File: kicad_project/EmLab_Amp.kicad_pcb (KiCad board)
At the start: 4 copper layers, 118.1 x 58 mm, 179 parts, among them J1 JTAG, J2 USB_C_Receptacle, J3 GPIO_EXP, J4 BNC, U1 TPS7A80, U10 THS4131ID, U11 THS4131ID, U12 THS4131ID, U2 LT3094xDD, U3 LT3045xDD, U4 TPS6513x, U5 LPC4370-TFBGA100, U6 IS25LP080D, U7 ADR421, U8 MCP601R, U9 LMH6518, Y1 12MHz Crystal

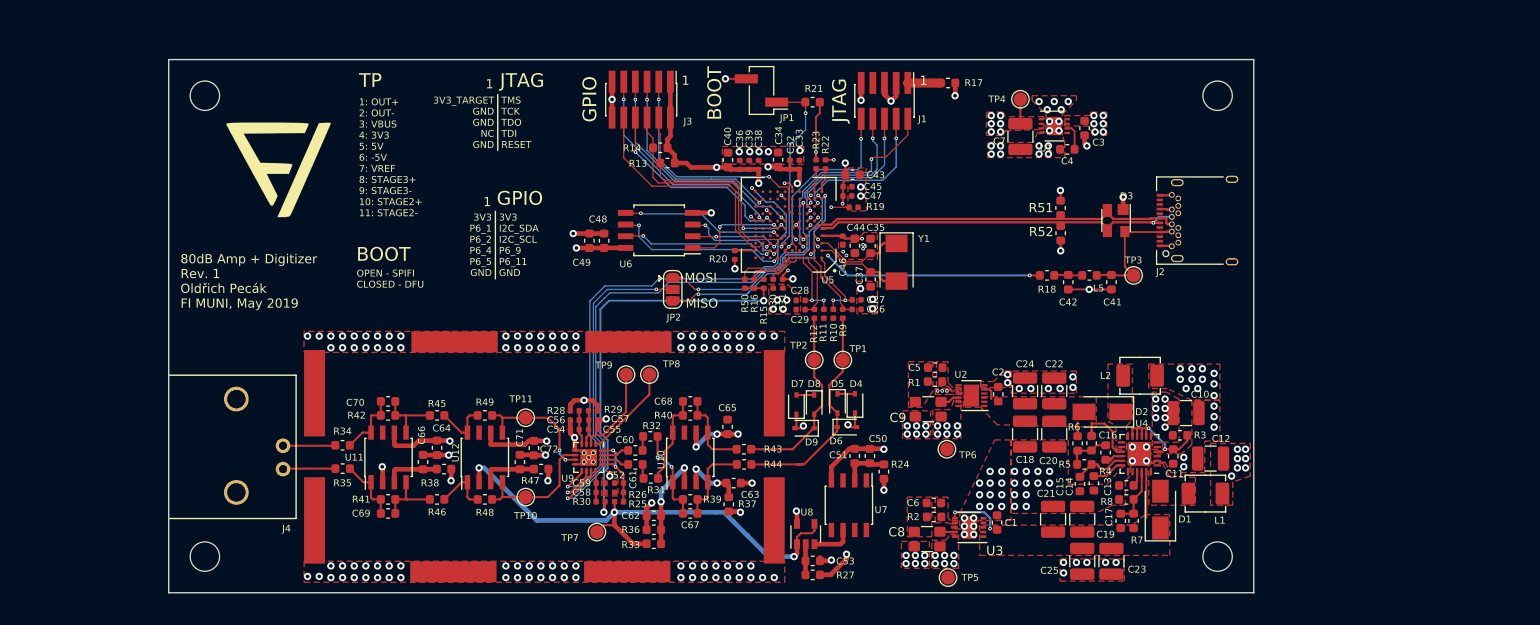
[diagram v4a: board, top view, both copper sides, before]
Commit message: PCB - add GND test points
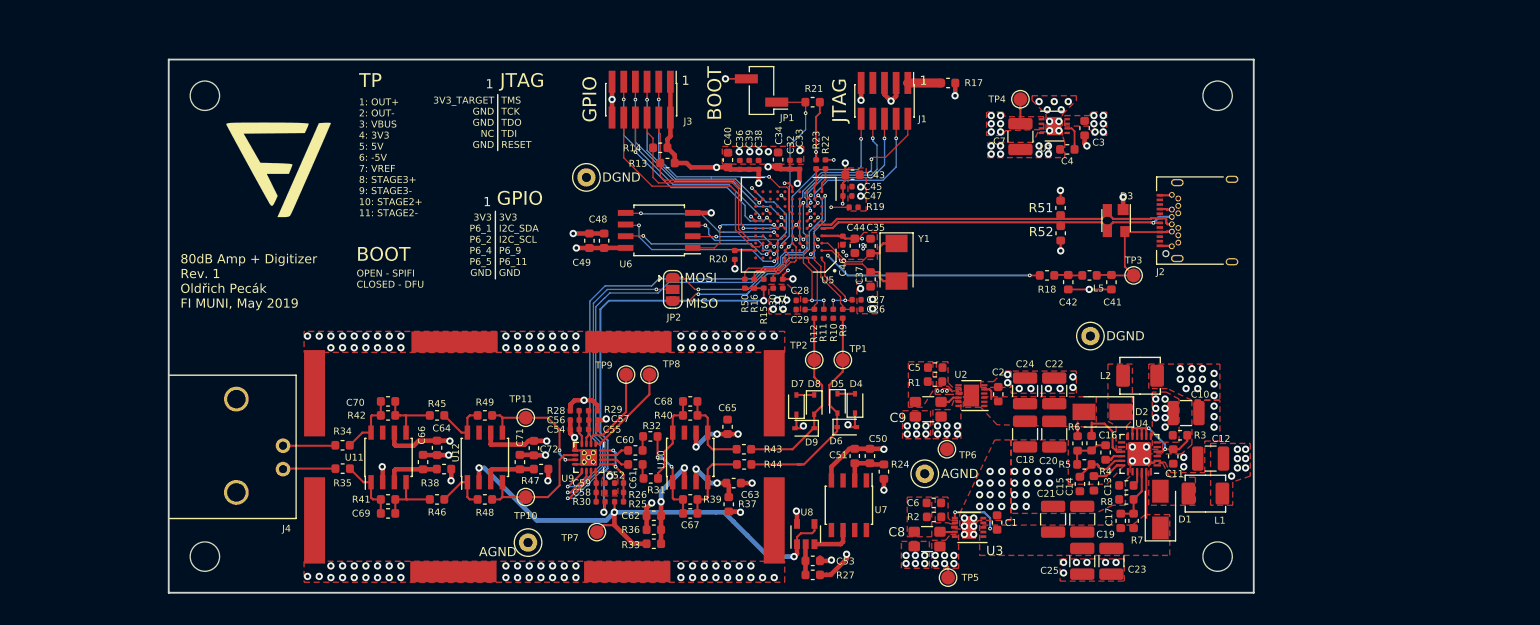
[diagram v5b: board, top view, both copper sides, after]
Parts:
- added AGND: TestPoint_Loop_D1.80mm_Drill1.0mm_Beaded, TestPoint:TestPoint_Loop_D1.80mm_Drill1.0mm_Beaded, F.Cu at (163.7, 105.7)
- added AGND: TestPoint_Loop_D1.80mm_Drill1.0mm_Beaded, TestPoint:TestPoint_Loop_D1.80mm_Drill1.0mm_Beaded, F.Cu at (120.5, 113.2)
- added DGND: TestPoint_Loop_D1.80mm_Drill1.0mm_Beaded, TestPoint:TestPoint_Loop_D1.80mm_Drill1.0mm_Beaded, F.Cu at (126.9, 73.4)
- added DGND: TestPoint_Loop_D1.80mm_Drill1.0mm_Beaded, TestPoint:TestPoint_Loop_D1.80mm_Drill1.0mm_Beaded, F.Cu at (181.7, 90.7)
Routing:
- net +5V: track 15.6 -> 17.3 mm
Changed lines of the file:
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@@
-(kicad_pcb (version 20171130) (host pcbnew "(5.0.0)")
+(kicad_pcb (version 20171130) (host pcbnew 5.0.0+dfsg1-2~bpo9+1)
   (general
     (thickness 1.6)
     (drawings 35)
-    (tracks 1476)
+    (tracks 1478)
     (zones 0)
-    (modules 179)
+    (modules 183)
     (nets 170)
   )
@@
   )
   (setup
-    (last_trace_width 0.244)
+    (last_trace_width 0.2)
     (user_trace_width 0.125)
     (user_trace_width 0.244)
@@
     (trace_min 0.125)
     (segment_width 0.15)
-    (edge_width 0.15)
+    (edge_width 0.2)
     (via_size 0.4)
     (via_drill 0.2)
@@
     (mod_text_size 0.75 0.75)
     (mod_text_width 0.135)
-    (pad_size 2.6 2.6)
-    (pad_drill 0)
+    (pad_size 2 2)
+    (pad_drill 1)
     (pad_to_mask_clearance 0.1)
     (solder_mask_min_width 0.15)
@@
     (add_net "Net-(U7-Pad8)")
   )
+  (module TestPoint:TestPoint_Loop_D1.80mm_Drill1.0mm_Beaded locked (layer F.Cu)
+    (at 126.873 73.406)
+    (descr "wire loop with bead as test point, loop diameter 1.8mm, hole diameter 1.0mm")
+    (tags "test point wire loop bead")
+    (fp_text reference DGND (at 3.81 0) (layer F.SilkS)
+      (effects (font (size 1 1) (thickness 0.15)))
+    )
+    (fp_text value TestPoint_Loop_D1.80mm_Drill1.0mm_Beaded (at 0 -2.8) (layer F.Fab)
+      (effects (font (size 1 1) (thickness 0.15)))
+    )
+    (fp_circle (center 0 0) (end 1.8 0) (layer F.CrtYd) (width 0.05))
+    (fp_circle (center 0 0) (end 1.5 0) (layer F.SilkS) (width 0.12))
+    (fp_line (start -0.9 -0.2) (end 0.9 -0.2) (layer F.Fab) (width 0.12))
+    (fp_line (start 0.9 -0.2) (end 0.9 0.2) (layer F.Fab) (width 0.12))
+    (fp_line (start 0.9 0.2) (end -0.9 0.2) (layer F.Fab) (width 0.12))
+    (fp_line (start -0.9 0.2) (end -0.9 -0.2) (layer F.Fab) (width 0.12))
+    (fp_circle (center 0 0) (end 1.3 0) (layer F.Fab) (width 0.12))
+    (fp_text user %R (at 0.7 2.5) (layer F.Fab)
+      (effects (font (size 1 1) (thickness 0.15)))
+    )
+    (pad 1 thru_hole circle (at 0 0) (size 2 2) (drill 1) (layers *.Cu *.Mask)
+      (net 19 GND))
+    (model ${KISYS3DMOD}/TestPoint.3dshapes/TestPoint_Loop_D1.80mm_Drill1.0mm_Beaded.wrl
+      (at (xyz 0 0 0))
+      (scale (xyz 1 1 1))
+      (rotate (xyz 0 0 0))
+    )
+  )
+  (module TestPoint:TestPoint_Loop_D1.80mm_Drill1.0mm_Beaded locked (layer F.Cu)
+    (at 181.737 90.678)
+    (descr "wire loop with bead as test point, loop diameter 1.8mm, hole diameter 1.0mm")
+    (tags "test point wire loop bead")
+    (fp_text reference DGND (at 3.81 0) (layer F.SilkS)
+      (effects (font (size 1 1) (thickness 0.15)))
+    )
+    (fp_text value TestPoint_Loop_D1.80mm_Drill1.0mm_Beaded (at 0 -2.8) (layer F.Fab)
+      (effects (font (size 1 1) (thickness 0.15)))
+    )
+    (fp_text user %R (at 0.7 2.5) (layer F.Fab)
+      (effects (font (size 1 1) (thickness 0.15)))
+    )
+    (fp_circle (center 0 0) (end 1.3 0) (layer F.Fab) (width 0.12))
+    (fp_line (start -0.9 0.2) (end -0.9 -0.2) (layer F.Fab) (width 0.12))
+    (fp_line (start 0.9 0.2) (end -0.9 0.2) (layer F.Fab) (width 0.12))
+    (fp_line (start 0.9 -0.2) (end 0.9 0.2) (layer F.Fab) (width 0.12))
+    (fp_line (start -0.9 -0.2) (end 0.9 -0.2) (layer F.Fab) (width 0.12))
+    (fp_circle (center 0 0) (end 1.5 0) (layer F.SilkS) (width 0.12))
+    (fp_circle (center 0 0) (end 1.8 0) (layer F.CrtYd) (width 0.05))
+    (pad 1 thru_hole circle (at 0 0) (size 2 2) (drill 1) (layers *.Cu *.Mask)
+      (net 19 GND))
+    (model ${KISYS3DMOD}/TestPoint.3dshapes/TestPoint_Loop_D1.80mm_Drill1.0mm_Beaded.wrl
+      (at (xyz 0 0 0))
+      (scale (xyz 1 1 1))
+      (rotate (xyz 0 0 0))
+    )
+  )
+  (module TestPoint:TestPoint_Loop_D1.80mm_Drill1.0mm_Beaded locked (layer F.Cu)
+    (at 163.703 105.664)
+    (descr "wire loop with bead as test point, loop diameter 1.8mm, hole diameter 1.0mm")
+    (tags "test point wire loop bead")
+    (fp_text reference AGND (at 3.81 0) (layer F.SilkS)
+      (effects (font (size 1 1) (thickness 0.15)))
+    )
+    (fp_text value TestPoint_Loop_D1.80mm_Drill1.0mm_Beaded (at 0 -2.8) (layer F.Fab)
+      (effects (font (size 1 1) (thickness 0.15)))
+    )
+    (fp_circle (center 0 0) (end 1.8 0) (layer F.CrtYd) (width 0.05))
+    (fp_circle (center 0 0) (end 1.5 0) (layer F.SilkS) (width 0.12))
+    (fp_line (start -0.9 -0.2) (end 0.9 -0.2) (layer F.Fab) (width 0.12))
+    (fp_line (start 0.9 -0.2) (end 0.9 0.2) (layer F.Fab) (width 0.12))
+    (fp_line (start 0.9 0.2) (end -0.9 0.2) (layer F.Fab) (width 0.12))
+    (fp_line (start -0.9 0.2) (end -0.9 -0.2) (layer F.Fab) (width 0.12))
+    (fp_circle (center 0 0) (end 1.3 0) (layer F.Fab) (width 0.12))
+    (fp_text user %R (at 0.7 2.5) (layer F.Fab)
+      (effects (font (size 1 1) (thickness 0.15)))
+    )
+    (pad 1 thru_hole circle (at 0 0) (size 2 2) (drill 1) (layers *.Cu *.Mask)
+      (net 19 GND))
+    (model ${KISYS3DMOD}/TestPoint.3dshapes/TestPoint_Loop_D1.80mm_Drill1.0mm_Beaded.wrl
+      (at (xyz 0 0 0))
+      (scale (xyz 1 1 1))
+      (rotate (xyz 0 0 0))
+    )
+  )
   (module MountingHole:MountingHole_3.2mm_M3 (layer F.Cu)
     (at 85.344 114.681)
@@
       (xy 5.063436 -5.054887) (xy 5.430622 -5.062373) (xy 5.666926 -5.040026)) (layer F.SilkS) (width 0.01))
   )
+  (module TestPoint:TestPoint_Loop_D1.80mm_Drill1.0mm_Beaded locked (layer F.Cu)
+    (at 120.523 113.157)
+    (descr "wire loop with bead as test point, loop diameter 1.8mm, hole diameter 1.0mm")
+    (tags "test point wire loop bead")
+    (fp_text reference AGND (at -3.302 1.016) (layer F.SilkS)
+      (effects (font (size 1 1) (thickness 0.15)))
+    )
+    (fp_text value TestPoint_Loop_D1.80mm_Drill1.0mm_Beaded (at 0 -2.8) (layer F.Fab)
+      (effects (font (size 1 1) (thickness 0.15)))
+    )
+    (fp_text user %R (at 0.7 2.5) (layer F.Fab)
+      (effects (font (size 1 1) (thickness 0.15)))
+    )
+    (fp_circle (center 0 0) (end 1.3 0) (layer F.Fab) (width 0.12))
+    (fp_line (start -0.9 0.2) (end -0.9 -0.2) (layer F.Fab) (width 0.12))
+    (fp_line (start 0.9 0.2) (end -0.9 0.2) (layer F.Fab) (width 0.12))
+    (fp_line (start 0.9 -0.2) (end 0.9 0.2) (layer F.Fab) (width 0.12))
+    (fp_line (start -0.9 -0.2) (end 0.9 -0.2) (layer F.Fab) (width 0.12))
+    (fp_circle (center 0 0) (end 1.5 0) (layer F.SilkS) (width 0.12))
+    (fp_circle (center 0 0) (end 1.8 0) (layer F.CrtYd) (width 0.05))
+    (pad 1 thru_hole circle (at 0 0) (size 2 2) (drill 1) (layers *.Cu *.Mask)
+      (net 19 GND))
+    (model ${KISYS3DMOD}/TestPoint.3dshapes/TestPoint_Loop_D1.80mm_Drill1.0mm_Beaded.wrl
+      (at (xyz 0 0 0))
+      (scale (xyz 1 1 1))
+      (rotate (xyz 0 0 0))
+    )
+  )
   (gr_text MISO (at 139.446 87.122) (layer F.SilkS)
     (effects (font (size 1 1) (thickness 0.2)))
@@
     (arrow2b (pts (xy 199.517 53.721) (xy 198.390496 54.307421)))
   )
-  (gr_line (start 199.517 118.618) (end 81.407 118.618) (layer Edge.Cuts) (width 0.15))
-  (gr_line (start 199.517 60.579) (end 199.517 118.618) (layer Edge.Cuts) (width 0.15))
-  (gr_line (start 81.407 60.579) (end 199.517 60.579) (layer Edge.Cuts) (width 0.15))
-  (gr_line (start 81.407 118.618) (end 81.407 60.579) (layer Edge.Cuts) (width 0.15))
+  (gr_line (start 199.517 118.618) (end 81.407 118.618) (layer Edge.Cuts) (width 0.2))
+  (gr_line (start 199.517 60.579) (end 199.517 118.618) (layer Edge.Cuts) (width 0.2))
+  (gr_line (start 81.407 60.579) (end 199.517 60.579) (layer Edge.Cuts) (width 0.2))
+  (gr_line (start 81.407 118.618) (end 81.407 60.579) (layer Edge.Cuts) (width 0.2))
   (gr_line (start 147.32 116.332) (end 147.32 91.313) (layer Dwgs.User) (width 0.2))
   (gr_line (start 97.282 116.332) (end 147.32 116.332) (layer Dwgs.User) (width 0.2))
@@
   (segment (start 153.459 116.67) (end 155.194 114.935) (width 0.5) (layer F.Cu) (net 8))
   (segment (start 155.194 114.935) (end 155.194 114.427) (width 0.5) (layer F.Cu) (net 8))
+  (segment (start 166.243 115.824) (end 165.862 115.443) (width 0.244) (layer F.Cu) (net 8))
+  (segment (start 166.243 116.967) (end 166.243 115.824) (width 0.244) (layer F.Cu) (net 8))
   (segment (start 128.81366 81.0768) (end 128.80086 81.0896) (width 0.5) (layer F.Cu) (net 9))
   (segment (start 131.14526 81.0768) (end 128.81366 81.0768) (width 0.5) (layer F.Cu) (net 9))
@@
       )
     )
+  )
+  (zone (net 0) (net_name "") (layer In2.Cu) (hatch edge 0.508)
+    (connect_pads (clearance 0.2))
+    (min_thickness 0.254)
+    (keepout (tracks not_allowed) (vias not_allowed) (copperpour not_allowed))
+    (fill (arc_segments 16) (thermal_gap 0.508) (thermal_bridge_width 0.508))
+    (polygon
+      (pts
+        (xy 141.605 100.711) (xy 141.605 101.981) (xy 140.462 101.981) (xy 139.065 103.378) (xy 138.176 103.378)
+        (xy 138.176 102.235) (xy 140.081 100.711)
+      )
+    )

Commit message: manufacturing files
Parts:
- AGND (x2), DGND (x2): value TestPoint_Loop_D1.80mm_Drill1.0mm_Beaded -> TestPoint_Loop_D2.54mm_Drill1.5mm_Beaded; footprint TestPoint:TestPoint_Loop_D1.80mm_Drill1.0mm_Beaded -> TestPoint:TestPoint_Loop_D2.54mm_Drill1.5mm_Beaded

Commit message: fix
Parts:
- J2: footprint Connector_USB:USB_C_Receptacle_Amphenol_12401548E4-2A -> Connector_USB:USB_C_Receptacle_Amphenol_12401610E4-2A
- moved R50 1.03 mm to (145.1, 85.0)
- moved R16 1.02 mm to (144.1, 85.0)
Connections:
- U4 pad 25: GND -> (no net)
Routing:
- net /LPC4370-JTAG-PWR-MISC/TRST: track 0.00 -> 6.49 mm, vias 0 -> 2
- net GND: track 79.8 -> 83.6 mm, vias 239 -> 238
- net +3V3: track 168.4 -> 166.4 mm
- net /LPC4370-USB/USB_VBUS: track 15.7 -> 17.6 mm, vias 20 -> 24
- net -5V: track 24.1 -> 25.8 mm
- net /LPC4370-JTAG-PWR-MISC/DBGEN: track 6.11 -> 5.10 mm
- net Net-(D3-Pad3): track 41.8 -> 42.6 mm, vias 1 -> 2
- net /LPC4370-JTAG-PWR-MISC/RESET: track 26.5 -> 27.2 mm
- net (no net): vias 0 -> 4

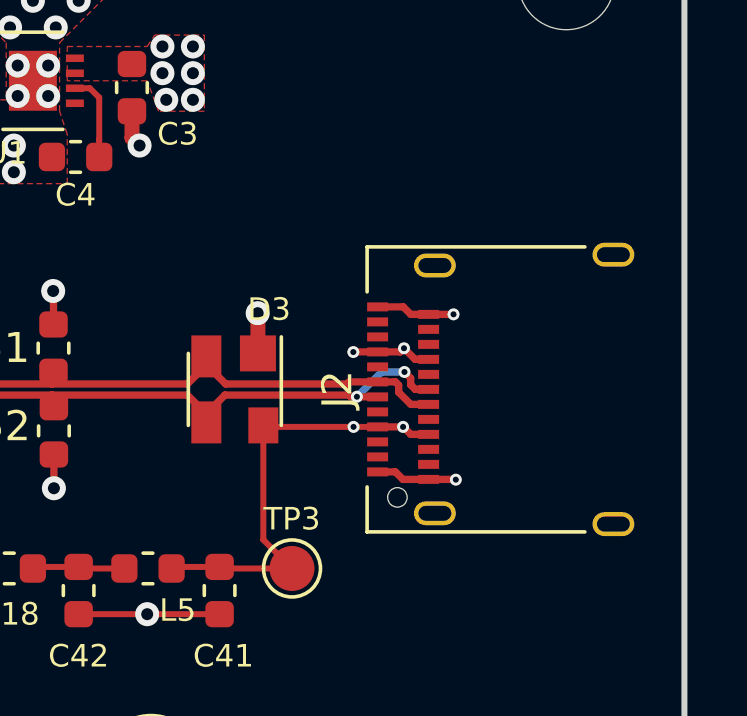
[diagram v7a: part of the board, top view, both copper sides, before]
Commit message: Change USB connector
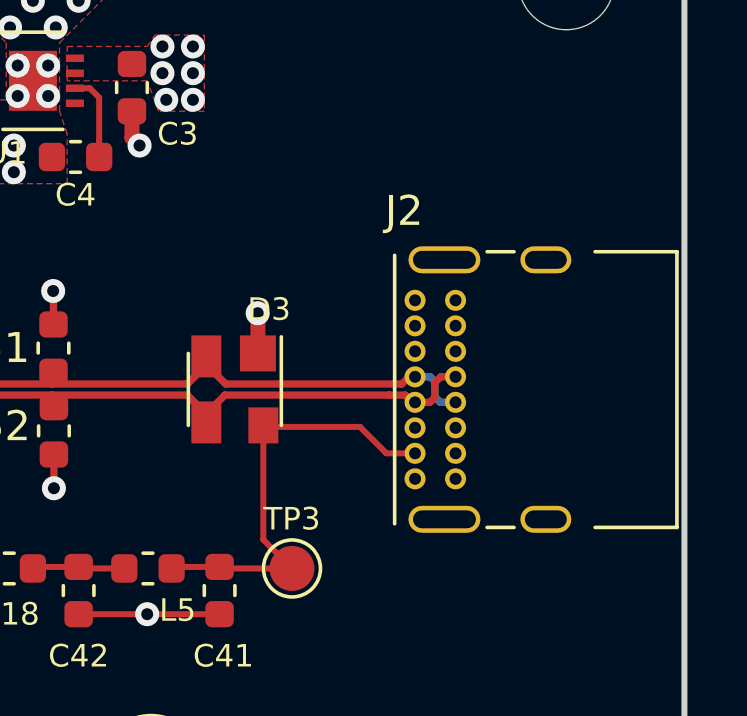
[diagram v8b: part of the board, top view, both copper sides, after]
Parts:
- J2: footprint Connector_USB:USB_C_Receptacle_Amphenol_12401610E4-2A -> Connector_USB:USB_C_Receptacle_GCT_USB4085
- moved J2 4.81 mm to (190.5, 81.1)
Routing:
- net GND: track 83.6 -> 78.3 mm, vias 238 -> 236
- net /LPC4370-USB/USB_VBUS: track 17.6 -> 14.7 mm, vias 24 -> 20
- net Net-(D3-Pad2): track 42.8 -> 44.0 mm
- net Net-(D3-Pad3): track 42.6 -> 42.8 mm, vias 2 -> 0
